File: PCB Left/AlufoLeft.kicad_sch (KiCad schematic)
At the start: 36 parts, among them J1 USB_C_Receptacle_USB2.0_16P_2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, J3 USB_C_Receptacle_USB2.0_16P_2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, J5 Shield_Connection, J7 Shield_Connection, J9 Shield_Connection, SW1 BOOT, U1 CH552T, U3 USBLC6-2P6, U5 USBLC6-2P6

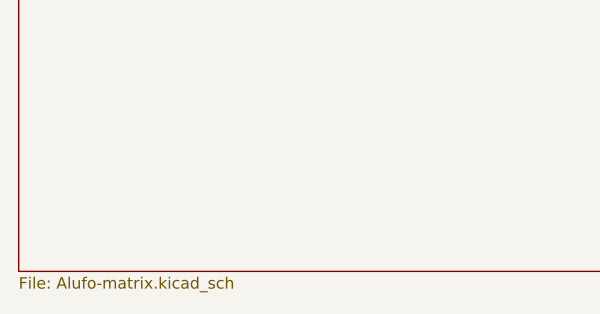
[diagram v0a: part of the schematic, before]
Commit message: Rename lefthand PCB project internally
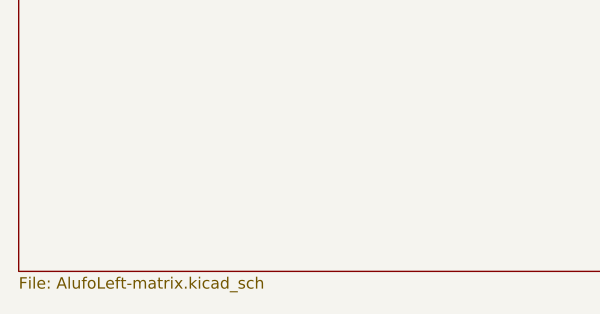
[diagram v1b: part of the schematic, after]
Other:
- sheet Matrix: file Alufo-matrix.kicad_sch -> AlufoLeft-matrix.kicad_sch
- title: Alufo  -> Alufo
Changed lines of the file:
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@@
 	(paper "A4" portrait)
 	(title_block
-		(title "Alufo ")
+		(title "Alufo")
 		(rev "1.1L")
 		(company "bgkendall")
@@
 		)
 		(instances
-			(project "Alufo"
+			(project "AlufoLeft"
 				(path "/52f043ac-ccff-4c85-bc10-2db9d3c9e3f3"
 					(reference "C1")
@@
 		)
 		(instances
-			(project "Alufo"
+			(project "AlufoLeft"
 				(path "/52f043ac-ccff-4c85-bc10-2db9d3c9e3f3"
 					(reference "H12")
@@
 		)
 		(instances
-			(project "Alufo"
+			(project "AlufoLeft"
 				(path "/52f043ac-ccff-4c85-bc10-2db9d3c9e3f3"
 					(reference "J7")
@@
 		)
 		(instances
-			(project "Alufo"
+			(project "AlufoLeft"
 				(path "/52f043ac-ccff-4c85-bc10-2db9d3c9e3f3"
 					(reference "H10")
@@
 		)
 		(instances
-			(project "Alufo"
+			(project "AlufoLeft"
 				(path "/52f043ac-ccff-4c85-bc10-2db9d3c9e3f3"
 					(reference "F1")
@@
 		)
 		(instances
-			(project "Alufo"
+			(project "AlufoLeft"
 				(path "/52f043ac-ccff-4c85-bc10-2db9d3c9e3f3"
 					(reference "#PWR04")
@@
 		)
 		(instances
-			(project "Alufo"
+			(project "AlufoLeft"
 				(path "/52f043ac-ccff-4c85-bc10-2db9d3c9e3f3"
 					(reference "H7")
@@
 		)
 		(instances
-			(project "Alufo"
+			(project "AlufoLeft"
 				(path "/52f043ac-ccff-4c85-bc10-2db9d3c9e3f3"
 					(reference "#PWR016")
@@
 		)
 		(instances
-			(project "Alufo"
+			(project "AlufoLeft"
 				(path "/52f043ac-ccff-4c85-bc10-2db9d3c9e3f3"
 					(reference "J9")
@@
 		)
 		(instances
-			(project "Alufo"
+			(project "AlufoLeft"
 				(path "/52f043ac-ccff-4c85-bc10-2db9d3c9e3f3"
 					(reference "#PWR019")
@@
 		)
 		(instances
-			(project "Alufo"
+			(project "AlufoLeft"
 				(path "/52f043ac-ccff-4c85-bc10-2db9d3c9e3f3"
 					(reference "C5")
@@
 		)
 		(instances
-			(project "Alufo"
+			(project "AlufoLeft"
 				(path "/52f043ac-ccff-4c85-bc10-2db9d3c9e3f3"
 					(reference "H8")
@@
 		)
 		(instances
-			(project "Alufo"
+			(project "AlufoLeft"
 				(path "/52f043ac-ccff-4c85-bc10-2db9d3c9e3f3"
 					(reference "D1")
@@
 		)
 		(instances
-			(project "Alufo"
+			(project "AlufoLeft"
 				(path "/52f043ac-ccff-4c85-bc10-2db9d3c9e3f3"
 					(reference "#PWR00")
@@
 		)
 		(instances
-			(project "Alufo"
+			(project "AlufoLeft"
 				(path "/52f043ac-ccff-4c85-bc10-2db9d3c9e3f3"
 					(reference "H11")
@@
 		)
 		(instances
-			(project "Alufo"
+			(project "AlufoLeft"
 				(path "/52f043ac-ccff-4c85-bc10-2db9d3c9e3f3"
 					(reference "#PWR011")
@@
 		)
 		(instances
-			(project "Alufo"
+			(project "AlufoLeft"
 				(path "/52f043ac-ccff-4c85-bc10-2db9d3c9e3f3"
 					(reference "H14")
@@
 		)
 		(instances
-			(project "Alufo"
+			(project "AlufoLeft"
 				(path "/52f043ac-ccff-4c85-bc10-2db9d3c9e3f3"
 					(reference "#PWR03")
@@
 		)
 		(instances
-			(project "Alufo"
+			(project "AlufoLeft"
 				(path "/52f043ac-ccff-4c85-bc10-2db9d3c9e3f3"
 					(reference "U5")
@@
 		)
 		(instances
-			(project "Alufo"
+			(project "AlufoLeft"
 				(path "/52f043ac-ccff-4c85-bc10-2db9d3c9e3f3"
 					(reference "#PWR014")
@@
 		)
 		(instances
-			(project "Alufo"
+			(project "AlufoLeft"
 				(path "/52f043ac-ccff-4c85-bc10-2db9d3c9e3f3"
 					(reference "#PWR015")
@@
 		)
 		(instances
-			(project "Alufo"
+			(project "AlufoLeft"
 				(path "/52f043ac-ccff-4c85-bc10-2db9d3c9e3f3"
 					(reference "#PWR018")
@@
 		)
 		(instances
-			(project "Alufo"
+			(project "AlufoLeft"
 				(path "/52f043ac-ccff-4c85-bc10-2db9d3c9e3f3"
 					(reference "#PWR010")
@@
 		)
 		(instances
-			(project "Alufo"
+			(project "AlufoLeft"
 				(path "/52f043ac-ccff-4c85-bc10-2db9d3c9e3f3"
 					(reference "R1")
@@
 		)
 		(instances
-			(project "Alufo"
+			(project "AlufoLeft"
 				(path "/52f043ac-ccff-4c85-bc10-2db9d3c9e3f3"
 					(reference "#PWR039")
@@
 		)
 		(instances
-			(project "Alufo"
+			(project "AlufoLeft"
 				(path "/52f043ac-ccff-4c85-bc10-2db9d3c9e3f3"
 					(reference "H6")
@@
 		)
 		(instances
-			(project "Alufo"
+			(project "AlufoLeft"
 				(path "/52f043ac-ccff-4c85-bc10-2db9d3c9e3f3"
 					(reference "#PWR013")
@@
 		)
 		(instances
-			(project "Alufo"
+			(project "AlufoLeft"
 				(path "/52f043ac-ccff-4c85-bc10-2db9d3c9e3f3"
 					(reference "C3")
@@
 		)
 		(instances
-			(project "Alufo"
+			(project "AlufoLeft"
 				(path "/52f043ac-ccff-4c85-bc10-2db9d3c9e3f3"
 					(reference "R5")
@@
 		)
 		(instances
-			(project "Alufo"
+			(project "AlufoLeft"
 				(path "/52f043ac-ccff-4c85-bc10-2db9d3c9e3f3"
 					(reference "#PWR020")
@@
 		)
 		(instances
-			(project "Alufo"
+			(project "AlufoLeft"
 				(path "/52f043ac-ccff-4c85-bc10-2db9d3c9e3f3"
 					(reference "#PWR022")
@@
 		)
 		(instances
-			(project "Alufo"
+			(project "AlufoLeft"
 				(path "/52f043ac-ccff-4c85-bc10-2db9d3c9e3f3"
 					(reference "#PWR038")
@@
 		)
 		(instances
-			(project "Alufo"
+			(project "AlufoLeft"
 				(path "/52f043ac-ccff-4c85-bc10-2db9d3c9e3f3"
 					(reference "#PWR01")
@@
 		)
 		(instances
-			(project "Alufo"
+			(project "AlufoLeft"
 				(path "/52f043ac-ccff-4c85-bc10-2db9d3c9e3f3"
 					(reference "#PWR05")
@@
 		)
 		(instances
-			(project "Alufo"
+			(project "AlufoLeft"
 				(path "/52f043ac-ccff-4c85-bc10-2db9d3c9e3f3"
 					(reference "#PWR021")
@@
 		)
 		(instances
-			(project "Alufo"
+			(project "AlufoLeft"
 				(path "/52f043ac-ccff-4c85-bc10-2db9d3c9e3f3"
 					(reference "H9")
@@
 		)
 		(instances
-			(project "Alufo"
+			(project "AlufoLeft"
 				(path "/52f043ac-ccff-4c85-bc10-2db9d3c9e3f3"
 					(reference "H13")
@@
 		)
 		(instances
-			(project "Alufo"
+			(project "AlufoLeft"
 				(path "/52f043ac-ccff-4c85-bc10-2db9d3c9e3f3"
 					(reference "#PWR09")
@@
 		)
 		(instances
-			(project "Alufo"
+			(project "AlufoLeft"
 				(path "/52f043ac-ccff-4c85-bc10-2db9d3c9e3f3"
 					(reference "#PWR06")
@@
 		)
 		(instances
-			(project "Alufo"
+			(project "AlufoLeft"
 				(path "/52f043ac-ccff-4c85-bc10-2db9d3c9e3f3"
 					(reference "R7")
@@
 		)
 		(instances
-			(project "Alufo"
+			(project "AlufoLeft"
 				(path "/52f043ac-ccff-4c85-bc10-2db9d3c9e3f3"
 					(reference "R3")
@@
 		)
 		(instances
-			(project "Alufo"
+			(project "AlufoLeft"
 				(path "/52f043ac-ccff-4c85-bc10-2db9d3c9e3f3"
 					(reference "R9")
@@
 		)
 		(instances
-			(project "Alufo"
+			(project "AlufoLeft"
 				(path "/52f043ac-ccff-4c85-bc10-2db9d3c9e3f3"
 					(reference "SW1")
@@
 		)
 		(instances
-			(project "Alufo"
+			(project "AlufoLeft"
 				(path "/52f043ac-ccff-4c85-bc10-2db9d3c9e3f3"
 					(reference "#PWR017")
@@
 		)
 		(instances
-			(project "Alufo"
+			(project "AlufoLeft"
 				(path "/52f043ac-ccff-4c85-bc10-2db9d3c9e3f3"
 					(reference "#PWR08")
@@
 		)
 		(instances
-			(project "Alufo"
+			(project "AlufoLeft"
 				(path "/52f043ac-ccff-4c85-bc10-2db9d3c9e3f3"
 					(reference "#PWR012")
@@
 			)
 		)
-		(property "Sheetfile" "Alufo-matrix.kicad_sch"
+		(property "Sheetfile" "AlufoLeft-matrix.kicad_sch"
 			(at 15.24 282.5246 0)
 			(effects
@@
 		)
 		(instances
-			(project "Alufo"
+			(project "AlufoLeft"
 				(path "/52f043ac-ccff-4c85-bc10-2db9d3c9e3f3"
 					(page "2")

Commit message: Remove plate from left and right PCBs
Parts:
- removed H10, H6, H7, H8, H9: ScrewHole, MountingHole:MountingHole_2.2mm_M2, symbol Mechanical:MountingHole
- removed H11, H12, H13, H14: Mousebites, Project_Library:Mousebites, symbol Mechanical:MountingHole
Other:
- moved on the sheet: H1, H2, H3, H4, H5, J9
